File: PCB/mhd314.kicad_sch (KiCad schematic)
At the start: 35 parts, among them J1 Raspberry_Pi_2_3, J2 AudioJack_Pentaconn, J4 AudioJack3_SwitchTR, SW1 SW_Push

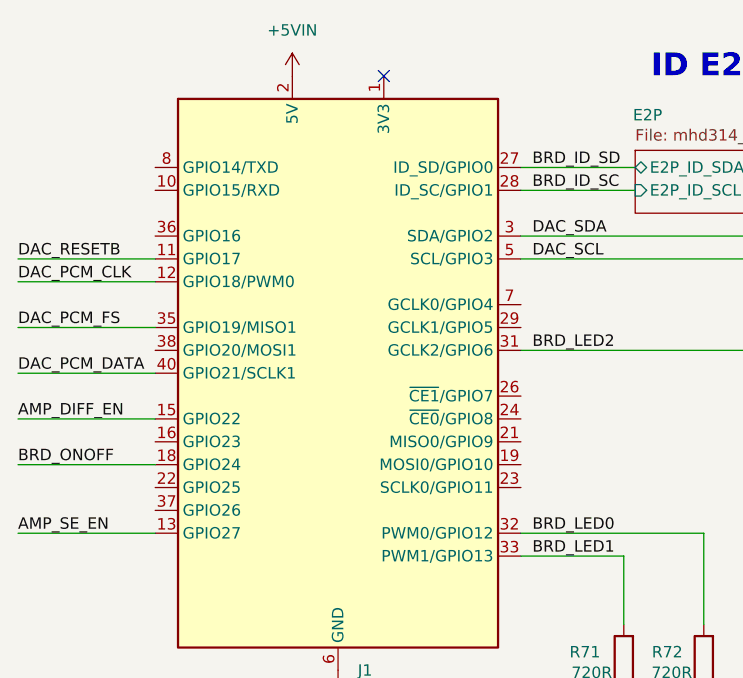
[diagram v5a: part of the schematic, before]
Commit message: Optimized designator positions and DNP for capacitors in OPA1622
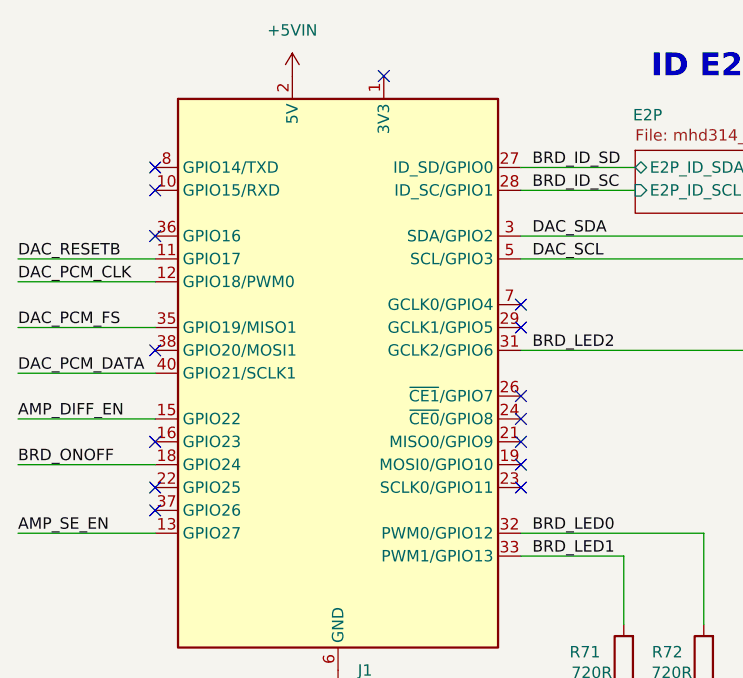
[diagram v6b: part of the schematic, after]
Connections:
- no-connect marks 8 -> 22
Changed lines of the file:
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@@
+	)
+	(no_connect
+		(at 36.83 92.71)
 	)
 	(no_connect
@@
 	)
 	(no_connect
+		(at 36.83 64.77)
+	)
+	(no_connect
+		(at 36.83 100.33)
+	)
+	(no_connect
+		(at 36.83 69.85)
+	)
+	(no_connect
+		(at 77.47 90.17)
+	)
+	(no_connect
 		(at 254 83.82)
+	)
+	(no_connect
+		(at 77.47 77.47)
+	)
+	(no_connect
+		(at 36.83 62.23)
+	)
+	(no_connect
+		(at 77.47 95.25)
+	)
+	(no_connect
+		(at 77.47 92.71)
+	)
+	(no_connect
+		(at 77.47 87.63)
+	)
+	(no_connect
+		(at 77.47 80.01)
+	)
+	(no_connect
+		(at 77.47 97.79)
 	)
 	(no_connect
@@
 	)
 	(no_connect
+		(at 36.83 82.55)
+	)
+	(no_connect
+		(at 36.83 97.79)
+	)
+	(no_connect

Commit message: Redone placement and layout of OPA1622. Still finishing touches
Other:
- sheet AMP ports: added AMP_IN_BAL_ENABLE; removed AMP_IN_BAL_L_ENABLE, AMP_IN_BAL_R_ENABLE
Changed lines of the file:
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@@
 	)
 	(junction
-		(at 189.23 64.77)
-		(diameter 0)
-		(color 0 0 0 0)
-	)
-	(junction
 		(at 97.79 134.62)
 		(diameter 0)
@@
 	(wire
 		(pts
-			(xy 189.23 62.23) (xy 189.23 64.77)
-		)
-		(stroke
-			(width 0)
-			(type default)
-		)
-	)
-	(wire
-		(pts
 			(xy 21.59 102.87) (xy 36.83 102.87)
 		)
@@
 	(wire
 		(pts
-			(xy 189.23 64.77) (xy 191.77 64.77)
-		)
-		(stroke
-			(width 0)
-			(type default)
-		)
-	)
-	(wire
-		(pts
 			(xy 198.12 105.41) (xy 195.58 105.41)
 		)
@@
 	(wire
 		(pts
-			(xy 175.26 64.77) (xy 189.23 64.77)
+			(xy 175.26 62.23) (xy 191.77 62.23)
 		)
 		(stroke
@@
 	(wire
 		(pts
-			(xy 191.77 62.23) (xy 189.23 62.23)
-		)
-		(stroke
-			(width 0)
-			(type default)
-		)
-	)
-	(wire
-		(pts
 			(xy 158.75 115.57) (xy 175.26 115.57)
 		)
@@
 	)
 	(label "AMP_DIFF_EN"
-		(at 175.26 64.77 0)
+		(at 175.26 62.23 0)
 		(effects
 			(font
@@
 			)
 		)
-		(pin "AMP_IN_BAL_R_ENABLE" input
-			(at 191.77 64.77 180)
-			(effects
-				(font
-					(size 1.27 1.27)
-				)
-				(justify left)
-			)
-		)
-		(pin "AMP_IN_BAL_L_ENABLE" input
+		(pin "AMP_IN_BAL_ENABLE" input
 			(at 191.77 62.23 180)
 			(effects

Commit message: Changed the BOM field for JLCPCB to the original name instead of LCSC
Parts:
- D3, D4: JLCPCB Part # (none) -> C2290; LCSC Part # C2290 -> (none)
- D5: JLCPCB Part # (none) -> C2286; LCSC Part # C2286 -> (none)
- J1: JLCPCB Part # (none) -> C132132; LCSC Part # C132132 -> (none)
- J2: JLCPCB Part # (none) -> C2762984; LCSC Part # C2762984 -> (none)
- J4: JLCPCB Part # (none) -> C22359743; LCSC Part # C22359743 -> (none)
- R71, R72, R73: JLCPCB Part # (none) -> C416571; LCSC Part # C416571 -> (none)
- SW1: JLCPCB Part # (none) -> C285519; LCSC Part # C285519 -> (none)
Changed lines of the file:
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@@
 			)
 		)
-		(property "LCSC Part #" "C416571"
+		(property "JLCPCB Part #" "C416571"
 			(at 97.79 116.84 0)
 			(effects
@@
 			)
 		)
-		(property "LCSC Part #" "C416571"
+		(property "JLCPCB Part #" "C416571"
 			(at 88.9 116.84 0)
 			(effects
@@
 			)
 		)
-		(property "LCSC Part #" "C2286"
+		(property "JLCPCB Part #" "C2286"
 			(at 107.95 127 0)
 			(effects
@@
 			)
 		)
-		(property "LCSC Part #" "C22359743"
+		(property "JLCPCB Part #" "C22359743"
 			(at 259.08 52.07 0)
 			(effects
@@
 			)
 		)
-		(property "LCSC Part #" "C285519"
+		(property "JLCPCB Part #" "C285519"
 			(at 119.38 116.84 0)
 			(effects
@@
 			)
 		)
-		(property "LCSC Part #" "C416571"
+		(property "JLCPCB Part #" "C416571"
 			(at 107.95 116.84 0)
 			(effects
@@
 			)
 		)
-		(property "LCSC Part #" "C2290"
+		(property "JLCPCB Part #" "C2290"
 			(at 97.79 127 0)
 			(effects
@@
 			)
 		)
-		(property "LCSC Part #" "C132132"
+		(property "JLCPCB Part #" "C132132"
 			(at 57.15 85.09 0)
 			(effects
@@
 			)
 		)
-		(property "LCSC Part #" "C2762984 "
+		(property "JLCPCB Part #" "C2762984 "
 			(at 259.08 72.39 0)
 			(effects
@@
 			)
 		)
-		(property "LCSC Part #" "C2290"
+		(property "JLCPCB Part #" "C2290"
 			(at 88.9 127 0)
 			(effects
